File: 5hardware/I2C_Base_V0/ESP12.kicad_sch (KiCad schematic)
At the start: 61 parts, among them J1 Conn_01x39_Socket, J4 Conn_01x39_Socket, P2 S4B-PH-SM4-TB, SW1 SW_Push, SW2 SW_Push, SW5 RotaryEncoder, U10 ESP-12F, U11 STM32L010F4Px, U12 APDS-9960, U14 DS3231M, U14 Lolin_Base, U2 ESP32-C3-WROOM-02, U5 SHT31-DIS, U6 DS1307Z+, U9 BH1750FVI-TR, U9 E18-MS1-PCB, Y1 Crystal, Y2 Crystal

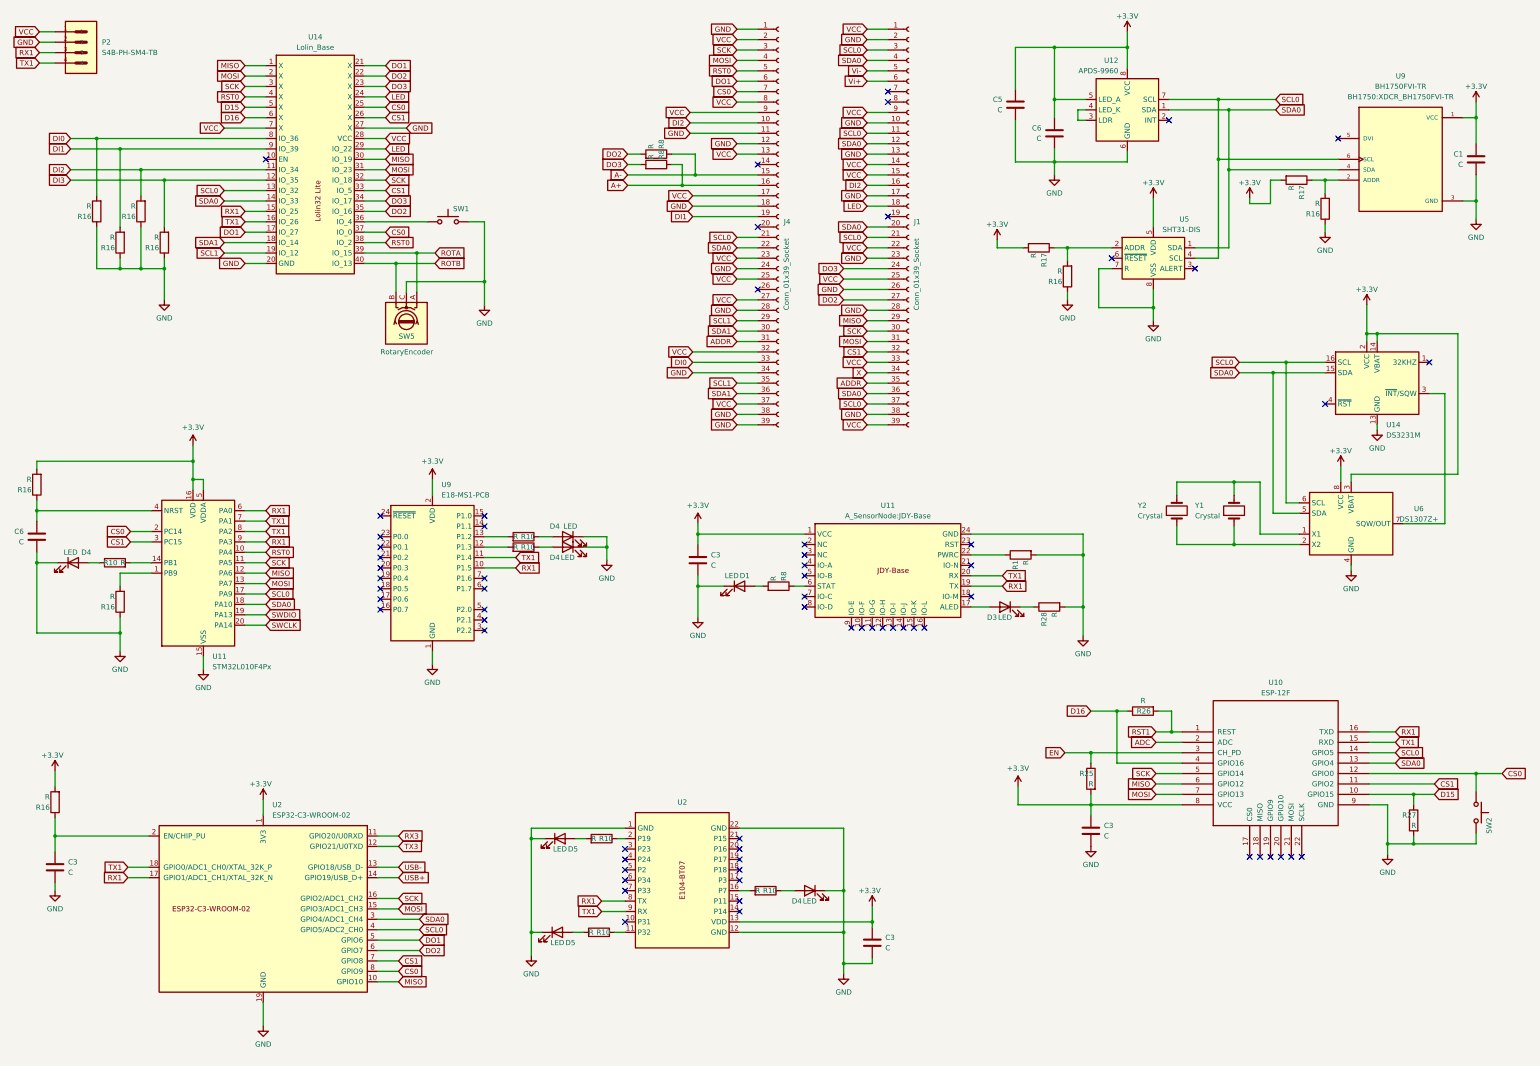
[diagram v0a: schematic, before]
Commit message: update schematic.
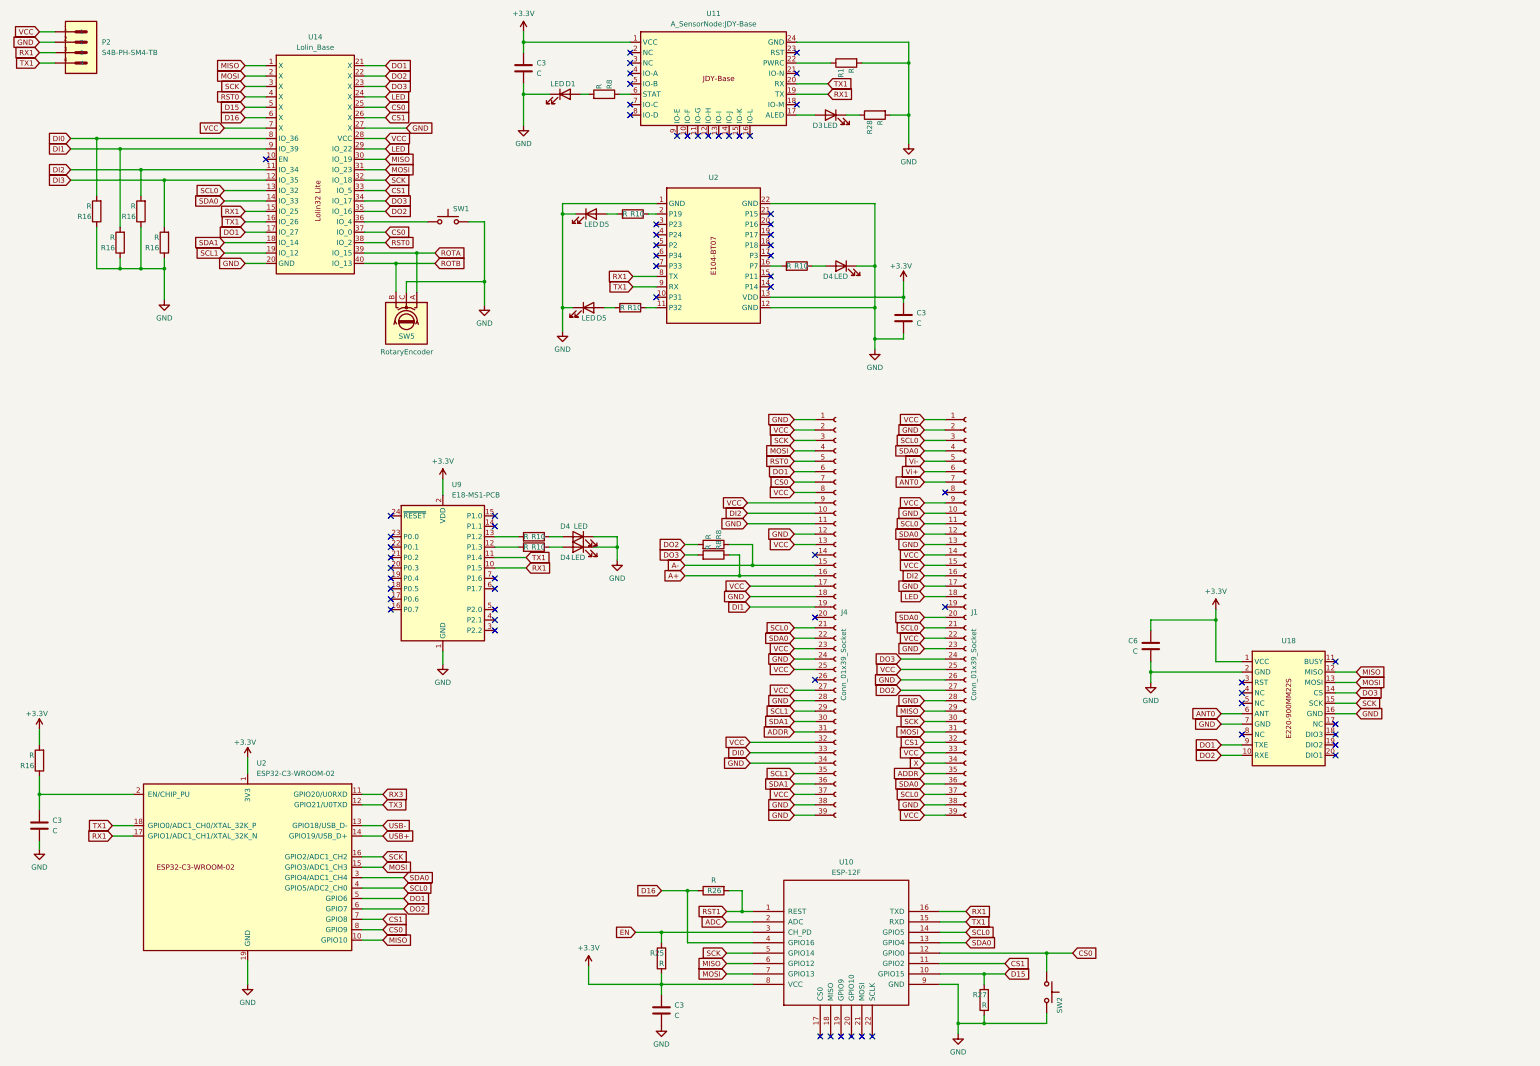
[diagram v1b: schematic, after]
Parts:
- removed C1, C5, C6 (x2): C, Capacitor_SMD:C_0805_2012Metric, symbol Device:C
- removed D4: LED, LED_SMD:LED_0603_1608Metric, symbol Device:LED
- removed R10, R16 (x2): R, Resistor_SMD:R_0805_2012Metric, symbol Device:R
- removed R16 (x2), R17 (x2): R, Resistor_SMD:R_0603_1608Metric, symbol Device:R
- removed U11: STM32L010F4Px, Package_SO:TSSOP-20_4.4x6.5mm_P0.65mm, symbol MCU_ST_STM32L0:STM32L010F4Px
- removed U12: APDS-9960, Sensor:Avago_APDS-9960, symbol Sensor:APDS-9960
- removed U14: DS3231M, Package_SO:SOIC-16W_7.5x10.3mm_P1.27mm, symbol Timer_RTC:DS3231M
- removed U5: SHT31-DIS, Sensor_Humidity:Sensirion_DFN-8-1EP_2.5x2.5mm_P0.5mm_EP1.1x1.7mm, symbol Sensor_Humidity:SHT31-DIS
- removed U6: DS1307Z+, Package_SO:SOIC-8_3.9x4.9mm_P1.27mm, symbol Timer_RTC:DS1307Z+
- removed U9: BH1750FVI-TR, BH1750:XDCR_BH1750FVI-TR, symbol BH1750FVI-TR:BH1750FVI-TR
- removed Y1: Crystal, Crystal:Crystal_SMD_3215-2Pin_3.2x1.5mm, symbol Device:Crystal
- removed Y2: Crystal, Crystal:Crystal_Round_D1.5mm_Vertical, symbol Device:Crystal
- added C6: C, Capacitor_SMD:C_0805_2012Metric, symbol Device:C
- added U18: ~, A_SensorNode:E220-900MM, symbol A_SensorNode:E220-900MM22S
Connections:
- net +3.3V: now also C6.1, U18.1 (VCC)
- net DO1: now also U18.9 (TXE)
- net DO2: now also U18.10 (RXE)
- net DO3: now also U18.14 (CS)
- net GND: now also C6.2, U18.16 (GND), U18.2 (GND), U18.7 (GND)
- net MISO: now also U18.12 (MISO)
- net MOSI: now also U18.13 (MOSI)
- net SCK: now also U18.15 (SCK)
- net ANT0: now reaches J1.7 (Pin_7)
- net ANT0: now also U18.6 (ANT)
- no-connect marks 65 -> 67
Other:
- moved on the sheet: C3, D1, D3, D4, D5, J1, J4, R1, R10, R16, R25, R26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

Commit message: update PCB.
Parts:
- added R26 (x4): R, Resistor_SMD:R_0805_2012Metric, symbol Device:R
- added U11: ~, A_SensorNode:JDY-41, symbol A_SensorNode:JDY-41
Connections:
- net RX3 is gone; now on net RX1: U2.11 (GPIO20/U0RXD)
- net TX3 is gone; now on net TX1: U2.12 (GPIO21/U0TXD)
- net +3.3V: now also U11.1 (VCC)
- net GND: now also U11.4 (SET), U11.5 (CS), U11.6 (GND)
- net RX1: now also R26.2, U11.3 (TX); no longer U10.16 (TXD), U2.17 (GPIO1/ADC1_CH1/XTAL_32K_N)
- net TX1: now also R26.2, U11.2 (RX); no longer U10.15 (RXD), U2.18 (GPIO0/ADC1_CH0/XTAL_32K_P)
- net USB+: no longer names the net of U2.14 (GPIO19/USB_D+)
- net USB-: no longer names the net of U2.13 (GPIO18/USB_D-)
- net X: no longer names the net of J1.34 (Pin_34)
- new net: R26.1, R26.1, U10.15 (RXD)
- new net: R26.1, R26.1, U10.16 (TXD)
- new net RX2: R26.2, U2.18 (GPIO0/ADC1_CH0/XTAL_32K_P)
- new net TX2: R26.2, U2.17 (GPIO1/ADC1_CH1/XTAL_32K_N)
- no-connect marks 67 -> 70
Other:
- moved on the sheet: C3, C6, D1, D3, D4, D5, J1, J4, P2, R1, R10, R16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
